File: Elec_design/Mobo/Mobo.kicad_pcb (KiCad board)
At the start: 2 copper layers, 95.2 x 141.2 mm, 40 parts, among them J1 6V_secteur, J10 Conn_01x04, J11 Conn_01x04, J12 Conn_01x04, J13 Conn_01x04, J14 Conn_01x04, J15 Conn_01x04, J16 Conn_01x04, J17 Conn_01x05, J2 Conn_batterie6V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

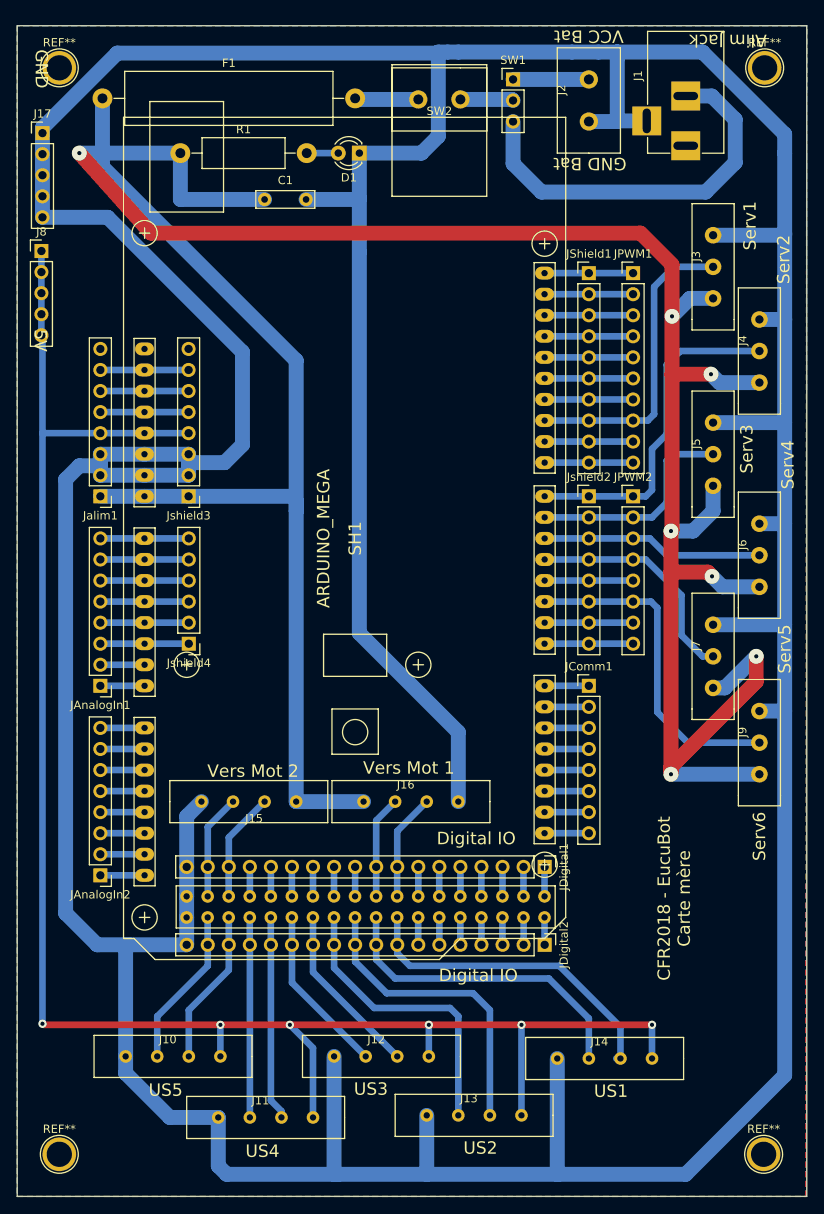
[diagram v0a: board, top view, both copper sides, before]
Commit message: Modification carte mère
Prise en compte de la taille des composants sur la carte
Modification d'empreinte
Ajustements
Ajout d'une led à programmer pour débugger
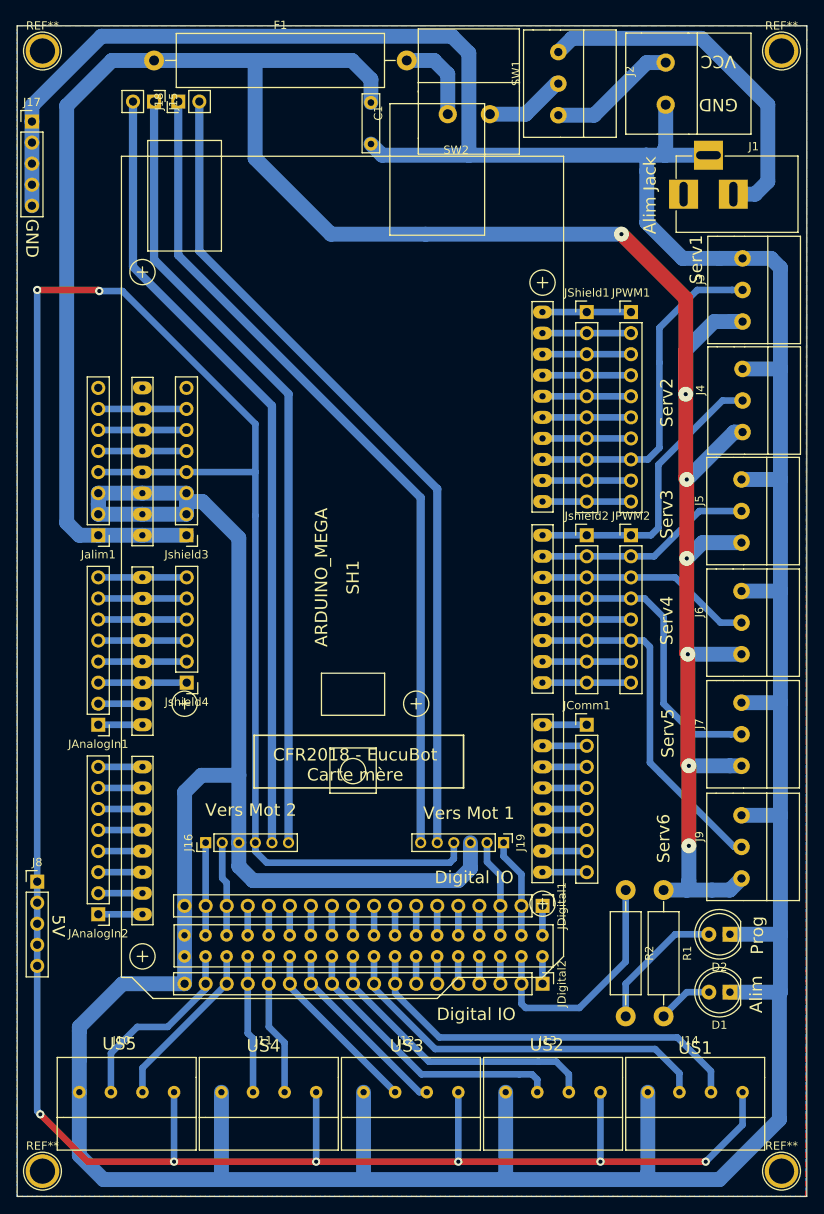
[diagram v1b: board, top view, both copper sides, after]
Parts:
- removed the REF** at (132.2, 165.1)
- removed the REF** at (47.2, 165.1)
- removed the REF** at (47.2, 34.0)
- removed the REF** at (132.3, 34.0)
- added D2: LED, LEDs:LED_D5.0mm, F.Cu at (128.1, 138.6)
- added J18: Conn_01x02, Pin_Headers:Pin_Header_Straight_1x02_Pitch2.54mm, F.Cu at (61.6, 38.1)
- added J19: Conn_01x06, Pin_Headers:Pin_Header_Straight_1x06_Pitch2.00mm, F.Cu at (100.8, 127.5)
- added R2: R, Resistors_THT:R_Axial_DIN0411_L9.9mm_D3.6mm_P15.24mm_Horizontal, F.Cu at (115.6, 133.2)
- added REF**: 1pin, Connectors:1pin, F.Cu at (45.2, 167.1)
- added REF**: 1pin, Connectors:1pin, F.Cu at (134.4, 167.1)
- added REF**: 1pin, Connectors:1pin, F.Cu at (45.2, 32.0)
- added REF**: 1pin, Connectors:1pin, F.Cu at (134.4, 32.0)
- D1: footprint LEDs:LED_D3.0mm -> LEDs:LED_D5.0mm
- J15: value Conn_01x04 -> Conn_01x02; footprint mylib:conn_4_3.81 -> Pin_Headers:Pin_Header_Straight_1x02_Pitch2.54mm
- J16: value Conn_01x04 -> Conn_01x06; footprint mylib:conn_4_3.81 -> Pin_Headers:Pin_Header_Straight_1x06_Pitch2.00mm
- SW1: footprint Pin_Headers:Pin_Header_Straight_1x03_Pitch2.54mm -> mylib:Conn_1x3_3.81
- SW2: footprint mylib:conn_01x02_5.08 -> mylib:conn_2_5.08
- moved D1 110.7 mm to (128.1, 145.5)
- moved R1 106.3 mm to (120.1, 133.2), turned to 270 degrees
- moved J15 87.8 mm to (58.7, 38.1), turned to 270 degrees
- moved J8 76.1 mm to (44.6, 132.2)
- moved J16 25.3 mm to (64.9, 127.5), turned to 90 degrees
- moved C1 17.4 mm to (84.8, 38.2), turned to 270 degrees
- moved J9 13.6 mm to (124.0, 126.7)
- moved J13 11.8 mm to (106.2, 150.9)
- moved J14 10.9 mm to (123.3, 150.9)
- moved J6 9.65 mm to (124.0, 99.7)
- moved J7 9.41 mm to (124.0, 113.2)
- moved J2 8.57 mm to (115.6, 34.4)
- moved J4 7.84 mm to (124.1, 72.9)
- moved F1 7.72 mm to (58.7, 33.1)
- moved J11 7.25 mm to (71.9, 150.9)
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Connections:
- J1 pad 1: (no net) -> Net-(J1-Pad1)
- J15 pad 1: /6V -> Net-(J15-Pad1)
- J15 pad 2: /50 -> Net-(J15-Pad2)
- J16 pad 1: /6V -> /52
- J16 pad 2: /36 -> /50
- J16 pad 3: /34 -> /GND
- J16 pad 4: /GND -> /5V
- Jalim1 pad 8: (no net) -> Net-(Jalim1-Pad8)
- Jshield3 pad 8: (no net) -> Net-(Jshield3-Pad8)
- SH1 pad NC: (no net) -> Net-(SH1-PadNC)
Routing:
- net /5V: track 219.4 -> 357.0 mm, vias 6 -> 8
- net Net-(J18-Pad1): track 0.00 -> 101.5 mm
- net Net-(J18-Pad2): track 0.00 -> 101.3 mm
- net /GND: track 697.0 -> 596.5 mm
- net Net-(J15-Pad2): track 0.00 -> 96.4 mm
- net Net-(J15-Pad1): track 0.00 -> 96.1 mm
- net /6V: track 368.4 -> 304.8 mm
- net /23: track 3.31 -> 29.5 mm
- net Net-(D2-Pad2): track 0.00 -> 16.4 mm
- net /35: track 39.2 -> 49.0 mm
- net /34: track 12.9 -> 3.56 mm
- net /36: track 12.4 -> 3.56 mm
- net /37: track 38.5 -> 47.2 mm
- net /22: track 3.56 -> 12.1 mm
- net /P5: track 28.5 -> 36.9 mm
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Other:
- net class Arduino: clearance 0.7 -> 0.4
- net class Default: clearance 0.7 -> 0.4
- net class Moteur added: clearance 0.4, trace_width 1, via_dia 1, via_drill 0.5
- rule trace_clearance: 0.7 -> 0.4
- board text added: "Alim"
- board text added: "Prog"
- board text added: "VCC"
- board text removed: "GND Bat"
- board text removed: "VCC Bat"
